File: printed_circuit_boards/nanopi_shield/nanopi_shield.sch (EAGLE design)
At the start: 4 parts, among them X1 1365-40

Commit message: Easier to solder and fix I2C
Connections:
- removed net I2C3_SCL: JP2.4, X1-7.S
- removed net I2C3_SDA: JP2.3, X1-9.S
- new net I2C2_SCL: JP2.4, X1-6.S
- new net I2C2_SDA: JP2.3, X1-4.S
- net N$2: now also X1-7.S; no longer X1-6.S
- net N$3: now also X1-9.S; no longer X1-4.S

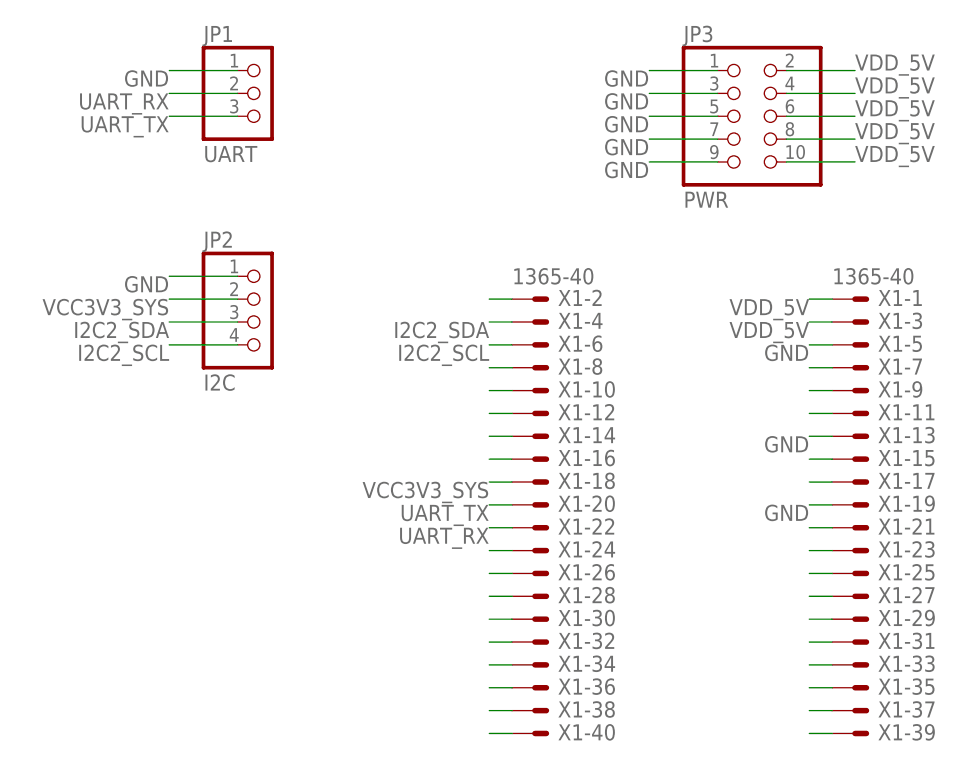
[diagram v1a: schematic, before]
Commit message: MPU9250 interrupt pin
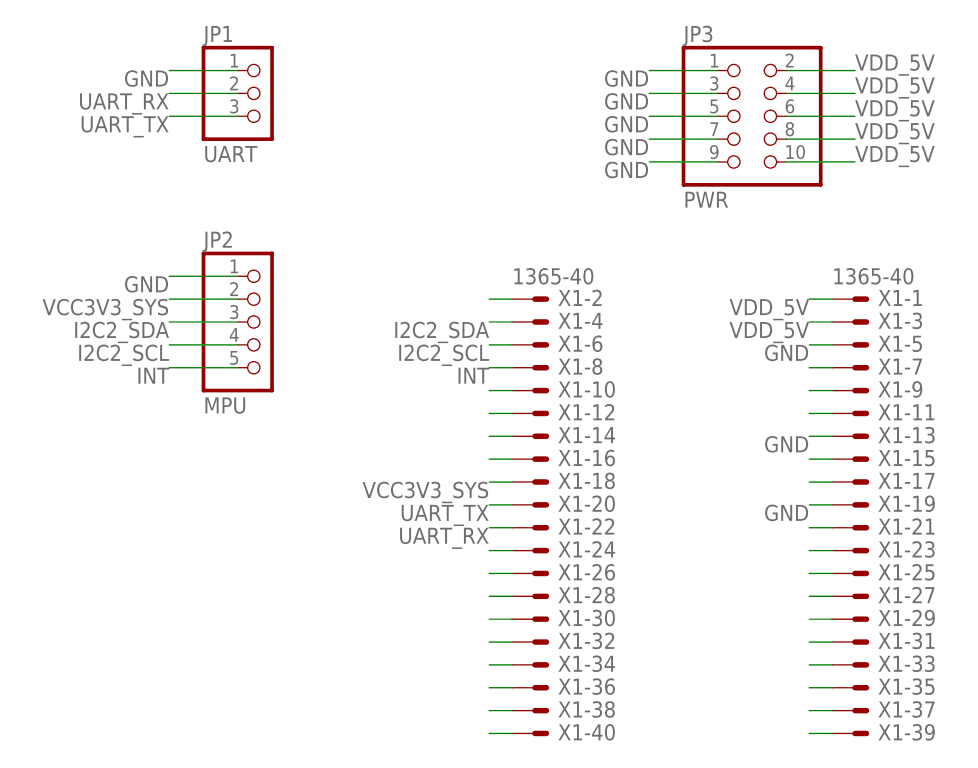
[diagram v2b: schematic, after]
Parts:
- JP2: value I2C -> MPU; device pinhead:PINHD-1X4 -> pinhead:PINHD-1X5
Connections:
- removed net N$1: X1-8.S
- new net INT: JP2.5, X1-8.S
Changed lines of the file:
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@@
 <parts>
 <part name="JP1" library="pinhead" library_urn="urn:adsk.eagle:library:325" deviceset="PINHD-1X3" device="" package3d_urn="urn:adsk.eagle:package:22458/2" value="UART"/>
-<part name="JP2" library="pinhead" library_urn="urn:adsk.eagle:library:325" deviceset="PINHD-1X4" device="" package3d_urn="urn:adsk.eagle:package:22407/2" value="I2C"/>
 <part name="JP3" library="pinhead" library_urn="urn:adsk.eagle:library:325" deviceset="PINHD-2X5" device="" package3d_urn="urn:adsk.eagle:package:22470/2" value="PWR"/>
 <part name="X1" library="con-leotronics" library_urn="urn:adsk.eagle:library:160" deviceset="1365-40" device="" package3d_urn="urn:adsk.eagle:package:7973/1"/>
+<part name="JP2" library="pinhead" library_urn="urn:adsk.eagle:library:325" deviceset="PINHD-1X5" device="" package3d_urn="urn:adsk.eagle:package:22469/2" value="MPU"/>
 </parts>
 <sheets>
@@
 <attribute name="VALUE" x="26.67" y="71.12" size="1.778" layer="96"/>
 </instance>
-<instance part="JP2" gate="A" x="33.02" y="53.34" smashed="yes">
-<attribute name="NAME" x="26.67" y="61.595" size="1.778" layer="95"/>
-<attribute name="VALUE" x="26.67" y="45.72" size="1.778" layer="96"/>
-</instance>
 <instance part="JP3" gate="A" x="86.36" y="76.2" smashed="yes">
 <attribute name="NAME" x="80.01" y="84.455" size="1.778" layer="95"/>
@@
 <instance part="X1" gate="-40" x="63.5" y="7.62" smashed="yes">
 <attribute name="NAME" x="66.04" y="6.858" size="1.778" layer="95"/>
+</instance>
+<instance part="JP2" gate="A" x="33.02" y="53.34" smashed="yes">
+<attribute name="NAME" x="26.67" y="61.595" size="1.778" layer="95"/>
+<attribute name="VALUE" x="26.67" y="43.18" size="1.778" layer="96"/>
 </instance>
 </instances>
@@
 </segment>
 <segment>
+<pinref part="X1" gate="-5" pin="S"/>
+<wire x1="96.52" y1="50.8" x2="93.98" y2="50.8" width="0.1524" layer="91"/>
+<label x="93.98" y="50.8" size="1.778" layer="95" rot="R180"/>
+</segment>
+<segment>
+<pinref part="X1" gate="-13" pin="S"/>
+<wire x1="96.52" y1="40.64" x2="93.98" y2="40.64" width="0.1524" layer="91"/>
+<label x="93.98" y="40.64" size="1.778" layer="95" rot="R180"/>
+</segment>
+<segment>
+<pinref part="X1" gate="-19" pin="S"/>
+<wire x1="96.52" y1="33.02" x2="93.98" y2="33.02" width="0.1524" layer="91"/>
+<label x="93.98" y="33.02" size="1.778" layer="95" rot="R180"/>
+</segment>
+<segment>
 <pinref part="JP2" gate="A" pin="1"/>
 <wire x1="30.48" y1="58.42" x2="22.86" y2="58.42" width="0.1524" layer="91"/>
 <label x="22.86" y="58.42" size="1.778" layer="95" rot="R180"/>
 </segment>
-<segment>
-<pinref part="X1" gate="-5" pin="S"/>
-<wire x1="96.52" y1="50.8" x2="93.98" y2="50.8" width="0.1524" layer="91"/>
-<label x="93.98" y="50.8" size="1.778" layer="95" rot="R180"/>
-</segment>
-<segment>
-<pinref part="X1" gate="-13" pin="S"/>
-<wire x1="96.52" y1="40.64" x2="93.98" y2="40.64" width="0.1524" layer="91"/>
-<label x="93.98" y="40.64" size="1.778" layer="95" rot="R180"/>
-</segment>
-<segment>
-<pinref part="X1" gate="-19" pin="S"/>
-<wire x1="96.52" y1="33.02" x2="93.98" y2="33.02" width="0.1524" layer="91"/>
-<label x="93.98" y="33.02" size="1.778" layer="95" rot="R180"/>
-</segment>
 </net>
 <net name="N$23" class="0">
@@
 </net>
 <net name="VCC3V3_SYS" class="0">
+<segment>
+<pinref part="X1" gate="-18" pin="S"/>
+<wire x1="60.96" y1="35.56" x2="58.42" y2="35.56" width="0.1524" layer="91"/>
+<label x="58.42" y="35.56" size="1.778" layer="95" rot="R180"/>
+</segment>
 <segment>
 <pinref part="JP2" gate="A" pin="2"/>
@@
 <label x="22.86" y="55.88" size="1.778" layer="95" rot="R180"/>
 </segment>
-<segment>
-<pinref part="X1" gate="-18" pin="S"/>
-<wire x1="60.96" y1="35.56" x2="58.42" y2="35.56" width="0.1524" layer="91"/>
-<label x="58.42" y="35.56" size="1.778" layer="95" rot="R180"/>
-</segment>
 </net>
 <net name="UART_TX" class="0">
@@
 </segment>
 </net>
-<net name="N$1" class="0">
-<segment>
-<pinref part="X1" gate="-8" pin="S"/>
-<wire x1="60.96" y1="48.26" x2="58.42" y2="48.26" width="0.1524" layer="91"/>
-</segment>
-</net>
 <net name="I2C2_SCL" class="0">
 <segment>
@@
 </segment>
 </net>
+<net name="INT" class="0">
+<segment>
+<pinref part="JP2" gate="A" pin="5"/>
+<wire x1="30.48" y1="48.26" x2="22.86" y2="48.26" width="0.1524" layer="91"/>
+<label x="22.86" y="48.26" size="1.778" layer="95" rot="R180"/>
+</segment>
+<segment>
+<pinref part="X1" gate="-8" pin="S"/>
+<wire x1="60.96" y1="48.26" x2="58.42" y2="48.26" width="0.1524" layer="91"/>
+<label x="58.42" y="48.26" size="1.778" layer="95" rot="R180"/>
+</segment>
+</net>
